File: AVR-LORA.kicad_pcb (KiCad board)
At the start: 2 copper layers, 34 parts, among them J1 Batt, J2 Solar, J3 CONN_01X01, J4 CONN_01X14, J5 CONN_01X14, U1 MCP1700-3302E_SOT23, U2 AVR128DB28, U3 RFM95HW, Y1 8MHz, Y2 32768Hz

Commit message: Layout AVR
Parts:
- C10: value 22pF -> 1uF
- C11: value 10pF -> 100nF
- C12: value 10pF -> 1uF
- C2: value 100nF -> 1uF
- C3, C4: value 1uF -> 22pF
- C5: value 100nF -> 10pF
- C6: value 1uF -> 10pF
- C9: value 22pF -> 100nF
- R1: value 100k -> 100R
- R2: value 100k -> 4K7
- R4: value 100R -> 1M
- R5: value 4K7 -> 1M
- U2: value AVR128DB28 -> RFM95HW; footprint Package_SO:SOIC-28W_7.5x17.9mm_P1.27mm -> RFM:RFM95
- U3: value RFM95HW -> AVR128DB28; footprint RFM:RFM95 -> Package_SO:SOIC-28W_7.5x17.9mm_P1.27mm
- Y1: value 8MHz -> 24MHz
- moved D1 80.3 mm to (-5.46, 143.4)
- moved J3 67.9 mm to (-5.84, 162.7)
- moved U1 62.4 mm to (-5.84, 168.3)
- moved R1 53.3 mm to (14.1, 164.5), turned to 270 degrees
- moved R3 52.9 mm to (15.6, 151.5)
- moved R4 49.8 mm to (16.8, 147.6), turned to 270 degrees
- moved J1 48.8 mm to (-5.84, 154.1)
- moved J2 47.7 mm to (-5.84, 150.0), turned to 180 degrees
- moved C10 46.2 mm to (15.6, 159.9)
- moved R2 45.4 mm to (15.6, 154.1)
- moved D2 44.2 mm to (14.1, 147.6), turned to 270 degrees
- moved C2 43.6 mm to (4.57, 165.7)
- moved JP5 43.2 mm to (9.27, 165.7)
- moved JP2 42.8 mm to (33.1, 147.4)
- moved C1 42.7 mm to (-0.51, 165.7)
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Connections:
- C10 pad 1: /A1 -> GND
- C10 pad 2: GND -> /3V3
- C11 pad 1: /F0 -> GND
- C11 pad 2: GND -> /3V3
- C12 pad 1: /F1 -> GND
- C12 pad 2: GND -> /3V3
- C2 pad 1: GND -> /3V3
- C2 pad 2: /3V3 -> GND
- C3 pad 1: GND -> /A0
- C3 pad 2: /3V3 -> GND
- C4 pad 1: /3V3 -> /A1
- C5 pad 1: GND -> /F0
- C5 pad 2: /3V3 -> GND
- C6 pad 1: GND -> /F1
- C6 pad 2: /3V3 -> GND
- C9 pad 1: /A0 -> GND
- C9 pad 2: GND -> /3V3
- JP1 pad 1: VCC -> /A0
- JP1 pad 2: /3V3 -> /CA0
- JP2 pad 1: /A0 -> /A1
- JP2 pad 2: /CA0 -> /CA1
- JP3 pad 1: /A1 -> /F0
- JP3 pad 2: /CA1 -> /CF0
- JP4 pad 1: /F0 -> /F1
- JP4 pad 2: /CF0 -> /CF1
- JP5 pad 1: /F1 -> VCC
- JP5 pad 2: /CF1 -> /3V3
- R1 pad 1: VCC -> /A7
- R1 pad 2: /D1 -> Net-(D2-Pad2)
- R2 pad 1: /D1 -> /3V3
- R2 pad 2: GND -> /A3
- R3 pad 2: /A3 -> /A2
- R4 pad 1: /A7 -> VCC
- R4 pad 2: Net-(D2-Pad2) -> /D1
- R5 pad 1: /3V3 -> /D1
- R5 pad 2: /A2 -> GND
- U2 pad 1: /A7 -> GND
- U2 pad 10: /D4 -> GND
- U2 pad 11: /D5 -> Net-(U2-Pad11)
- U2 pad 12: /D6 -> Net-(U2-Pad12)
- U2 pad 13: /D7 -> /3V3
- U2 pad 14: /3V3 -> /D2
- U2 pad 15: GND -> /D3
- U2 pad 16: /F0 -> /D4
- U2 pad 2: /C0 -> /A5
- U2 pad 3: /C1 -> /A4
- U2 pad 4: /C2 -> /A6
- U2 pad 5: /C3 -> /D6
- U2 pad 6: /3V3 -> /D5
- U2 pad 7: /D1 -> Net-(U2-Pad7)
- U2 pad 8: /D2 -> GND
- U2 pad 9: /D3 -> Net-(J3-Pad1)
- U3 pad 1: GND -> /A7
- U3 pad 10: GND -> /D4
- U3 pad 11: Net-(U3-Pad11) -> /D5
- U3 pad 12: Net-(U3-Pad12) -> /D6
- U3 pad 13: /3V3 -> /D7
- U3 pad 14: /D2 -> /3V3
- U3 pad 15: /D3 -> GND
- U3 pad 16: /D4 -> /F0
- U3 pad 2: /A5 -> /C0
- U3 pad 3: /A4 -> /C1
- U3 pad 4: /A6 -> /C2
- U3 pad 5: /D6 -> /C3
- U3 pad 6: /D5 -> /3V3
- U3 pad 7: Net-(U3-Pad7) -> /D1
- U3 pad 8: GND -> /D2
- U3 pad 9: Net-(J3-Pad1) -> /D3

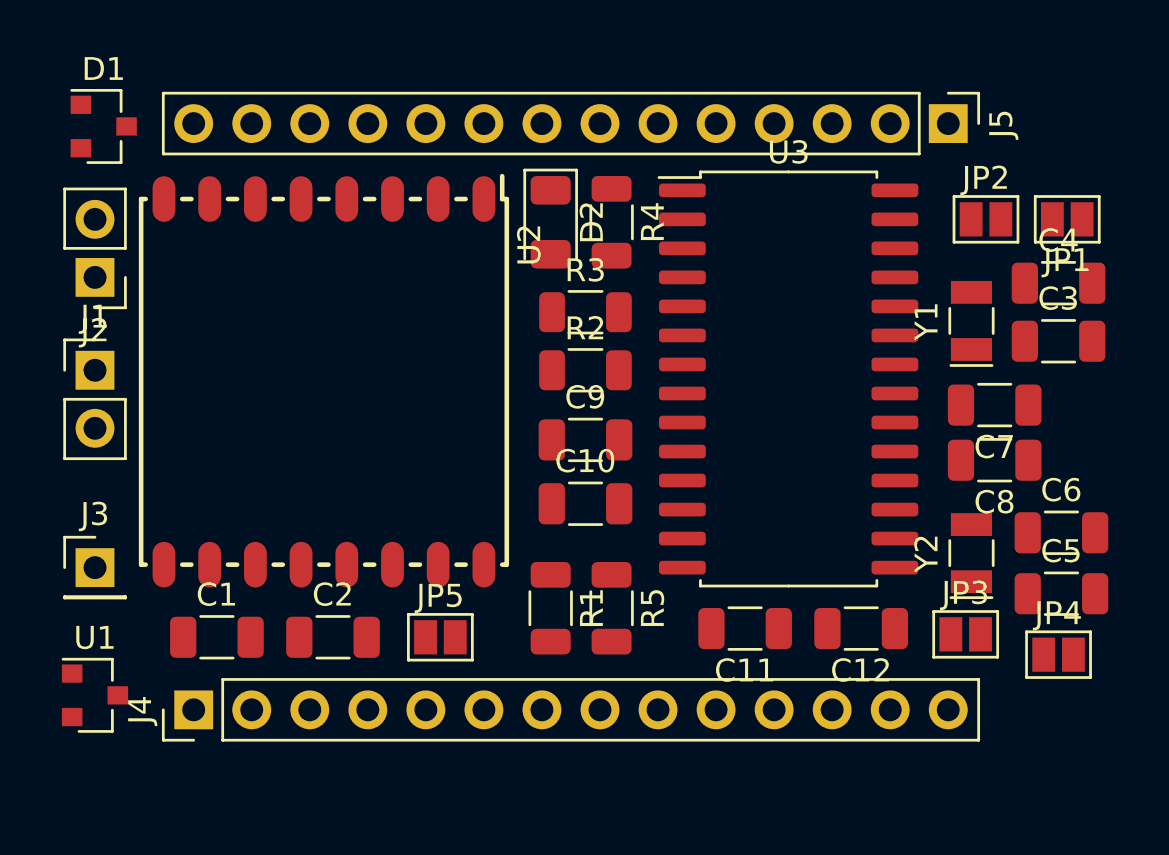
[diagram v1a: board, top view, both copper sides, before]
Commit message: Start routing AVR
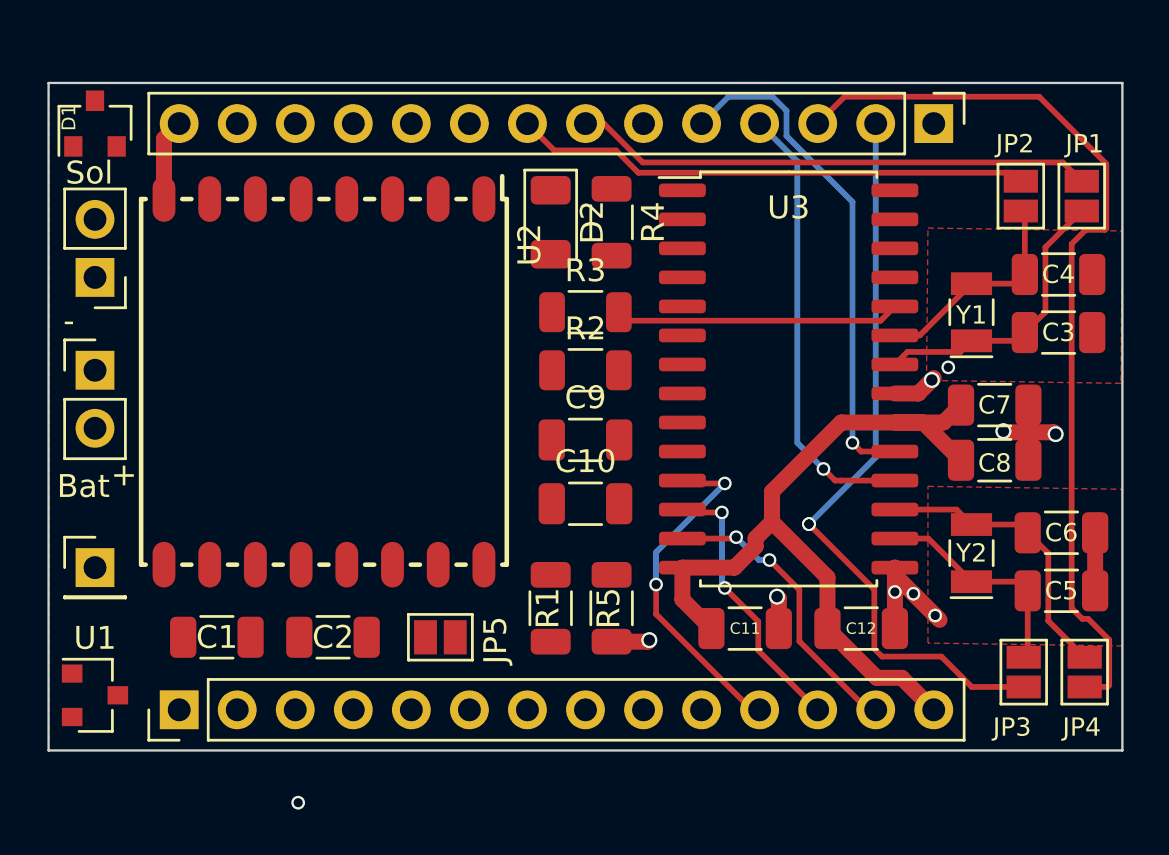
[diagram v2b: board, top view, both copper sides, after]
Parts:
- moved JP3 3.03 mm to (34.8, 167.3), turned to 270 degrees
- moved JP2 1.83 mm to (34.7, 146.4), turned to 90 degrees
- moved JP4 1.37 mm to (37.5, 167.3), turned to 270 degrees
- moved JP1 1.20 mm to (37.3, 146.4), turned to 90 degrees
- moved J4 0.63 mm to (-2.16, 168.9)
- moved J5 0.63 mm to (30.9, 143.3)
- moved D1 0.40 mm to (-5.84, 143.3), turned to 90 degrees
- moved C3 0.38 mm to (36.3, 152.4)
- moved C4 0.38 mm to (36.3, 149.9)
- moved Y1 0.38 mm to (32.5, 151.5)
- moved C5 0.13 mm to (36.4, 163.7)
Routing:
- net /CF1: track 0.00 -> 40.2 mm
- net /3V3: track 0.00 -> 34.7 mm
- net /CF0: track 0.00 -> 32.6 mm, vias 0 -> 2
- net /CA0: track 0.00 -> 22.8 mm
- net /CA1: track 0.00 -> 22.6 mm
- net /UPDI: track 0.00 -> 22.2 mm, vias 0 -> 1
- net GND: track 0.00 -> 21.7 mm, vias 0 -> 9
- net /F6: track 0.00 -> 19.6 mm, vias 0 -> 1
- net /D5: track 0.00 -> 15.1 mm, vias 0 -> 2
- net /D7: track 0.00 -> 12.9 mm, vias 0 -> 2
- net /F1: track 0.00 -> 12.7 mm
- net /A0: track 0.00 -> 12.6 mm
- net /A2: track 0.00 -> 12.5 mm
- net /D6: track 0.00 -> 12.2 mm, vias 0 -> 2
- net /F0: track 0.00 -> 9.74 mm
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- added copper zone on B.Cu, net GND
- added copper zone on F.Cu, net GND
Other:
- board outline added: 47 x 29.2 mm
- board text added: "+"
- board text added: "-"
- board text added: "Bat"
- board text added: "Sol"

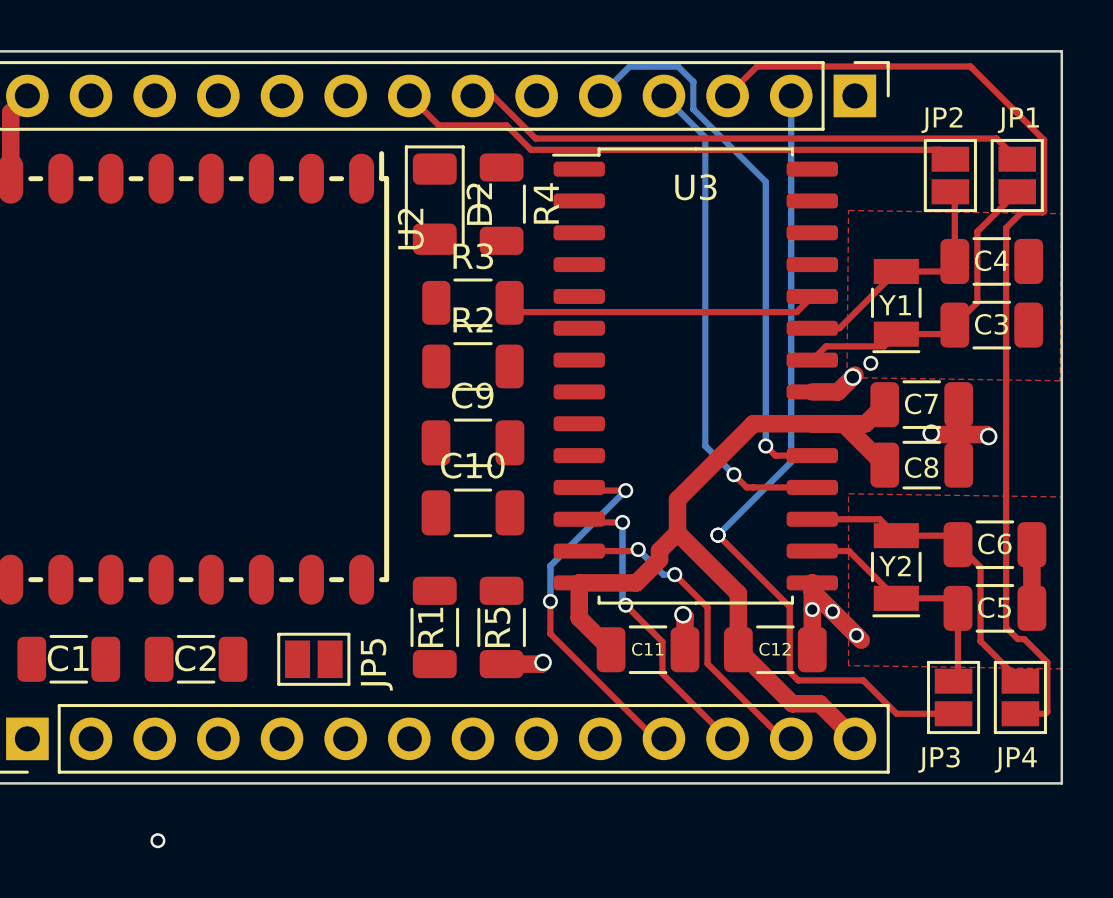
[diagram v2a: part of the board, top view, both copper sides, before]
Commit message: Start routing AVR
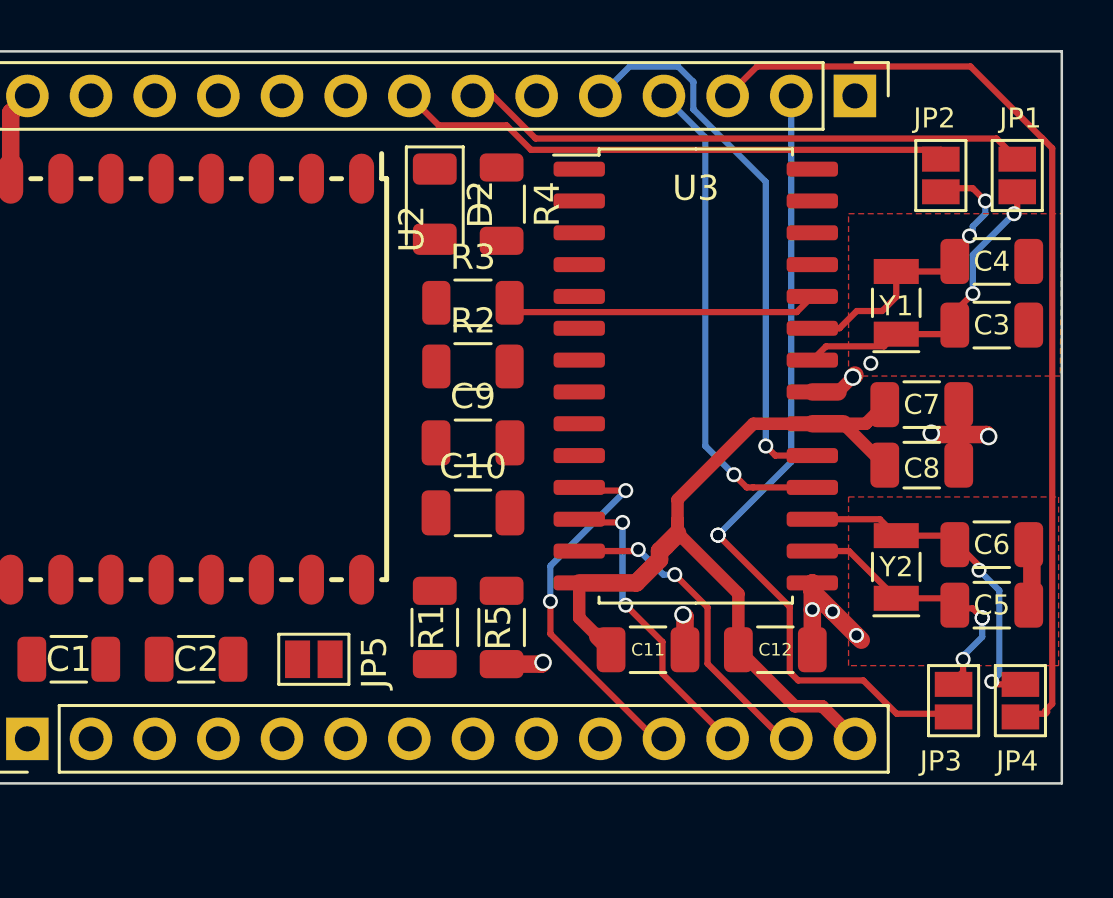
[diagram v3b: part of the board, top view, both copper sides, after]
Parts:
- moved JP2 0.38 mm to (34.3, 146.4)
- moved C5 0.18 mm to (36.3, 163.6)
- moved JP3 0.13 mm to (34.8, 167.4)
- moved JP4 0.13 mm to (37.5, 167.4)
- moved C6 0.13 mm to (36.3, 161.2)
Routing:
- net /3V3: track 34.7 -> 40.4 mm
- net /A1: track 9.64 -> 12.6 mm, vias 0 -> 2
- net /CF1: track 40.2 -> 38.7 mm
- net /F0: track 9.74 -> 11.1 mm, vias 0 -> 3
- net /F1: track 12.7 -> 13.7 mm, vias 0 -> 2
- net /A0: vias 0 -> 2
- net (no net): vias 1 -> 0
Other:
- net class Power: trace_width 0.7 -> 0.5

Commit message: Clean DRC AVR
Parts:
- moved R4 17.1 mm to (14.1, 164.5)
- moved R1 17.1 mm to (16.9, 147.6)
- moved R2 2.54 mm to (15.6, 151.5)
- moved R3 2.54 mm to (15.6, 154.1)
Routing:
- net /3V3: track 40.4 -> 111.6 mm, vias 0 -> 1
- net VCC: track 0.00 -> 54.3 mm, vias 0 -> 2
- net GND: track 21.7 -> 68.7 mm, vias 9 -> 21
- net /C0: track 0.00 -> 37.9 mm, vias 0 -> 3
- net /C3: track 0.00 -> 37.7 mm, vias 0 -> 2
- net /A7: track 0.00 -> 34.7 mm, vias 0 -> 6
- net /C1: track 0.00 -> 33.3 mm, vias 0 -> 3
- net /A6: track 0.00 -> 32.6 mm, vias 0 -> 2
- net /A4: track 0.00 -> 31.8 mm, vias 0 -> 1
- net /A5: track 0.00 -> 30.9 mm, vias 0 -> 2
- net /D3: track 0.00 -> 29.9 mm, vias 0 -> 4
- net /A3: track 0.00 -> 29.8 mm, vias 0 -> 1
- net /C2: track 0.00 -> 29.1 mm, vias 0 -> 3
- net /D2: track 0.00 -> 28.3 mm, vias 0 -> 4
- net /D4: track 0.00 -> 27.1 mm, vias 0 -> 4
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
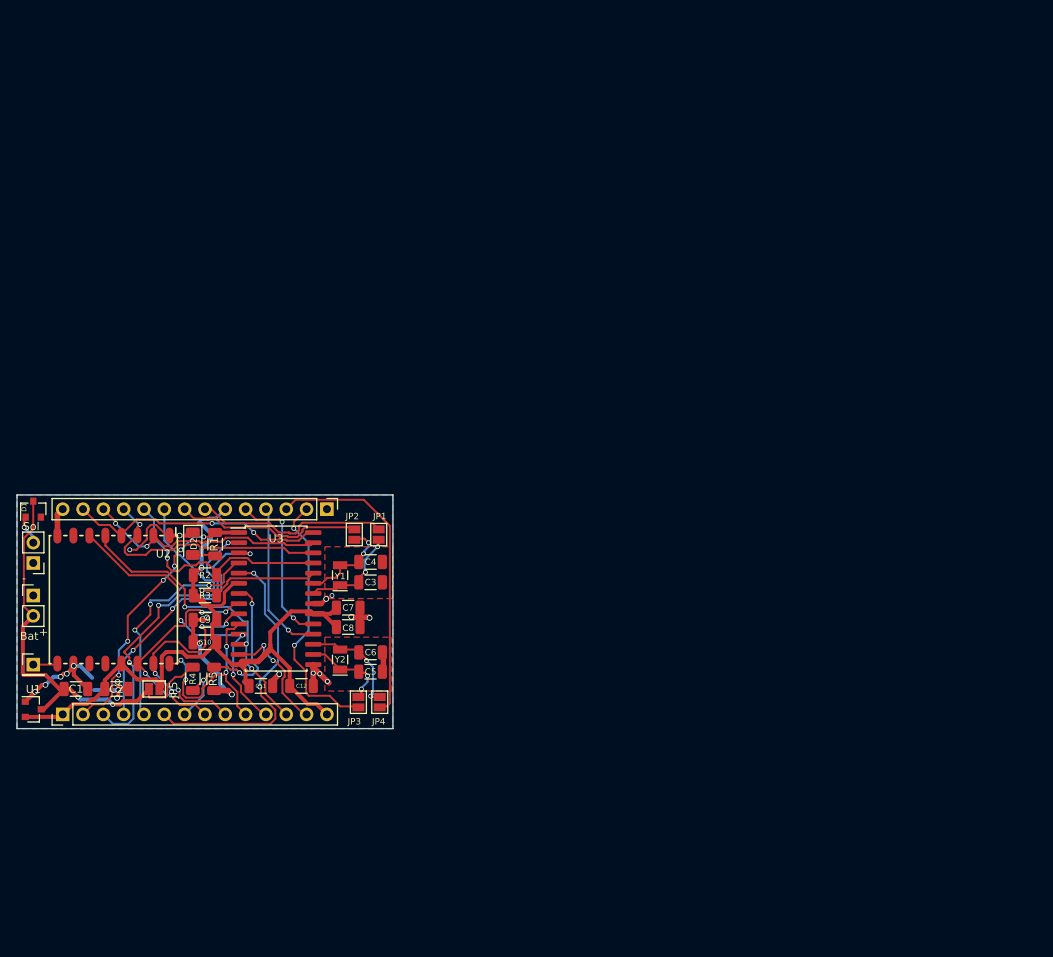
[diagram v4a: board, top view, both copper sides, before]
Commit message: Cleanup and add pin labels AVR
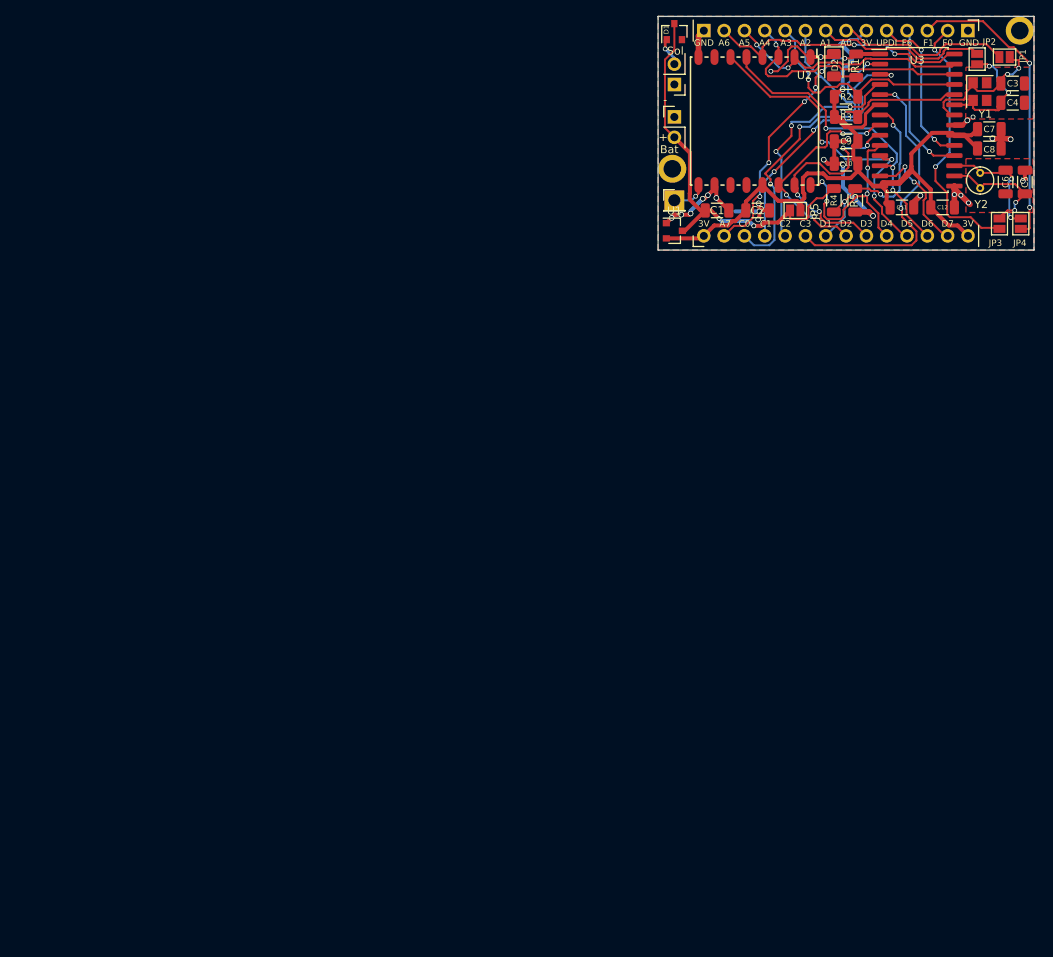
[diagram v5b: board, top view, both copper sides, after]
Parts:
- added REF**: MountingHole_2.2mm_M2_ISO7380_Pad, MountingHole:MountingHole_2.2mm_M2_ISO7380_Pad, F.Cu at (74.0, 100.7)
- added REF**: MountingHole_2.2mm_M2_ISO7380_Pad, MountingHole:MountingHole_2.2mm_M2_ISO7380_Pad, F.Cu at (117.5, 83.4)
- C3, C4: value 22pF -> 20pF
- C5, C6: value 10pF -> 12pF
- Y1: footprint Crystal:Crystal_SMD_MicroCrystal_CC7V-T1A-2Pin_3.2x1.5mm -> Crystal:Crystal_SMD_Abracon_ABM8G-4Pin_3.2x2.5mm
- Y2: footprint Crystal:Crystal_SMD_MicroCrystal_CC7V-T1A-2Pin_3.2x1.5mm -> Crystal:Crystal_Round_D3.0mm_Vertical
- moved C5 102.2 mm to (118.1, 102.4), turned to 90 degrees
- moved C3 101.6 mm to (116.6, 90.0)
- moved Y1 100.2 mm to (112.5, 91.1), turned to 270 degrees
- moved C1 100.0 mm to (79.6, 105.9)
- moved C10 100.0 mm to (95.8, 100.1)
- moved C11 100.0 mm to (102.7, 105.5)
- moved C12 100.0 mm to (107.8, 105.5)
- moved C2 100.0 mm to (84.7, 105.9)
- moved D2 100.0 mm to (94.2, 87.8)
- moved J5 100.0 mm to (111.0, 83.4)
- moved JP5 100.0 mm to (89.4, 105.9)
- moved R4 100.0 mm to (94.2, 104.6)
- moved R5 100.0 mm to (96.9, 104.6)
- moved U1 100.0 mm to (74.3, 108.5)
- moved C7 100.0 mm to (113.7, 95.8)
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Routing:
- net /F0: track 11.1 -> 16.0 mm
- net /A0: track 12.6 -> 17.3 mm
- net /A1: track 12.6 -> 17.2 mm
- net VCC: track 54.3 -> 51.6 mm
- net /CA1: track 23.8 -> 21.3 mm
- net /D5: track 39.3 -> 41.7 mm
- net /CA0: track 24.2 -> 21.8 mm
- net Net-(J3-Pad1): track 3.07 -> 4.60 mm, vias 0 -> 1
- net /CF1: track 38.7 -> 37.4 mm, vias 0 -> 2
- net GND: track 68.7 -> 67.6 mm, vias 21 -> 24
- net /F1: track 13.7 -> 14.8 mm
- net /D6: track 38.9 -> 39.8 mm
- net /A6: track 32.6 -> 33.3 mm
- net /3V3: track 111.6 -> 112.3 mm
- net /UPDI: track 20.6 -> 20.0 mm
- added copper zone on F.Cu, net /3V3
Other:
- board text added: "3V"
- board text added: "A0"
- board text added: "A1"
- board text added: "A2"
- board text added: "A3"
- board text added: "A4"
- board text added: "A5"
- board text added: "A6"
- board text added: "A7"
- board text added: "C0"
- board text added: "C1"
- board text added: "C2"
- board text added: "C3"
- board text added: "D1"
- board text added: "D2"
- board text added: "D3"
- board text added: "D4"
- board text added: "D5"
- board text added: "D6"
- board text added: "D7"
- board text added: "F0"
- board text added: "F1"
- board text added: "F6"
- board text added: "GND"
- board text added: "UPDI"
